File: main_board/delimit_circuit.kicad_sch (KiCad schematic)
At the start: 18 parts, among them J1 Conn_02x24_Counter_Clockwise, J2 Conn_02x24_Counter_Clockwise, J5 Screw_Terminal_01x02, J6 Screw_Terminal_01x02, J7 Screw_Terminal_01x02, J8 Screw_Terminal_01x02, U1 LTV-817, U2 LTV-817, U3 LTV-817, U4 LTV-817

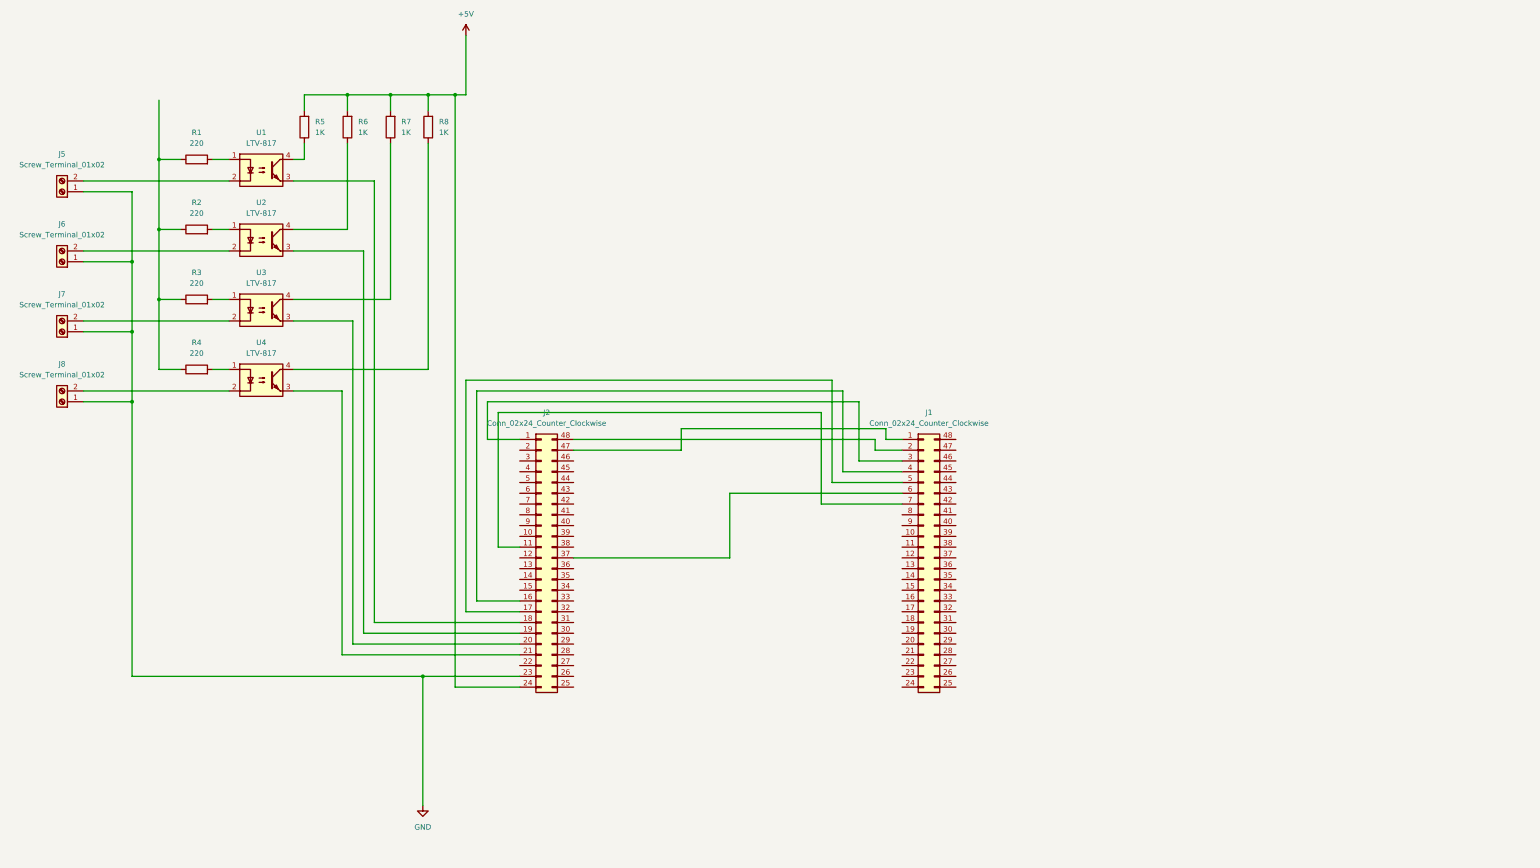
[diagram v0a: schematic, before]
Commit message: made teensy symbol
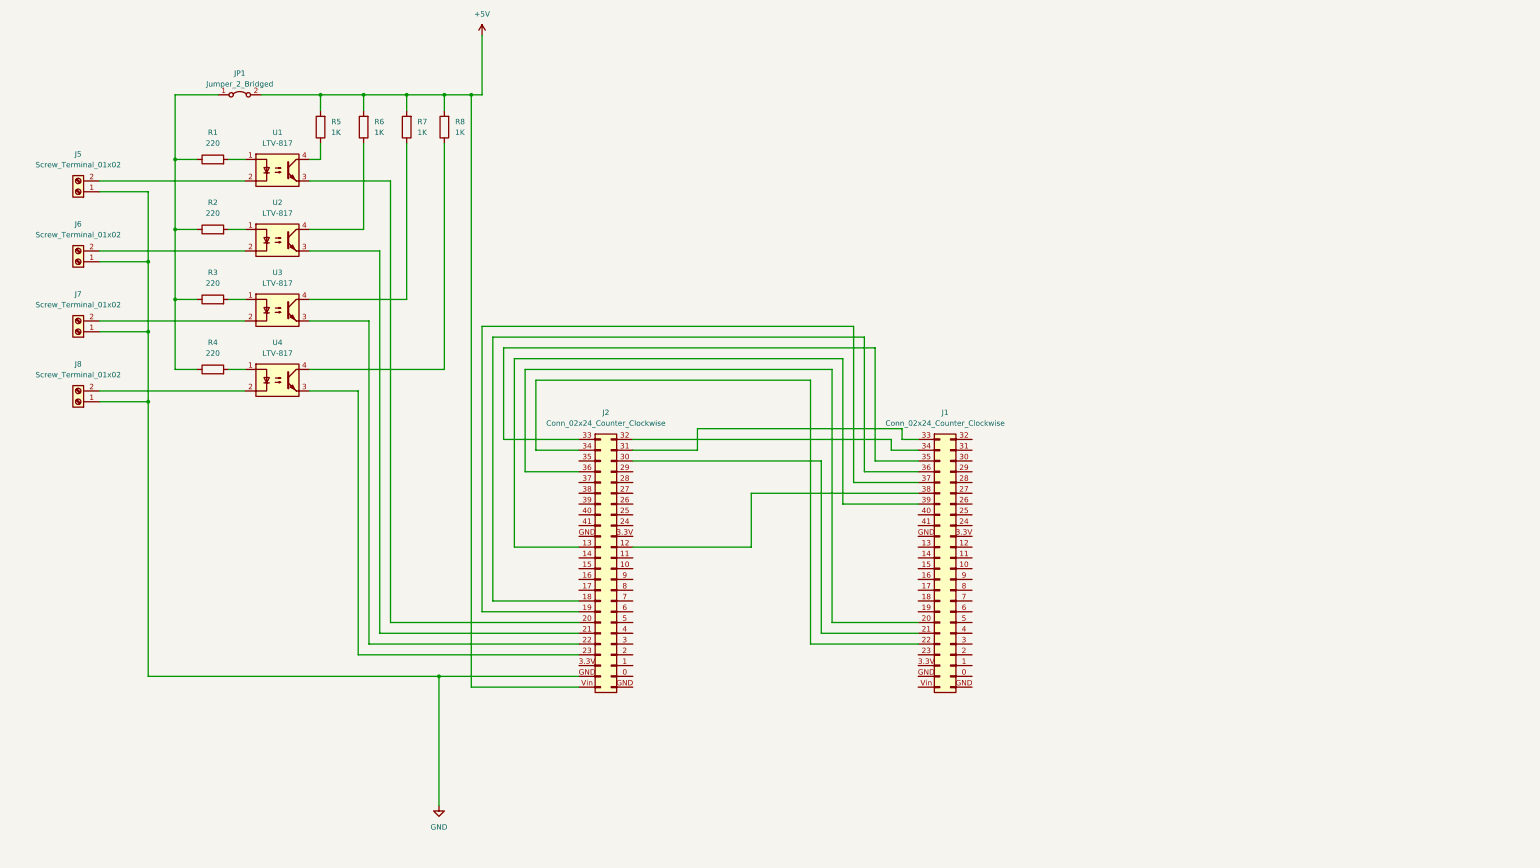
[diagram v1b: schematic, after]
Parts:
- added JP1: Jumper_2_Bridged, Jumper:SolderJumper-2_P1.3mm_Bridged2Bar_Pad1.0x1.5mm, symbol Jumper:Jumper_2_Bridged
- J1, J2: symbol Connector_Generic:Conn_02x24_Counter_Clockwise -> delimit:teensy_4_1_conn_02x24
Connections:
- net +5V: now also J2.Vin (Pin_Vin), JP1.2 (B); no longer J2.24 (Pin_24)
- net GND: now also J2.GND (Pin_GND); no longer J2.23 (Pin_23)
- net at R1.1, R2.1, R3.1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: now also JP1.1 (A)
- net at J2.1 (Pin_1): no longer J1.3 (Pin_3)
- net at J2.11 (Pin_11): no longer J1.7 (Pin_7)
- net at J2.12 (Pin_12): now also J1.38 (Pin_38)
- net at J2.13 (Pin_13): now also J1.39 (Pin_39)
- net at J2.16 (Pin_16): no longer J1.4 (Pin_4)
- net at J2.17 (Pin_17): no longer J1.5 (Pin_5)
- net at J2.18 (Pin_18): now also J1.36 (Pin_36); no longer U1.3
- net at J2.19 (Pin_19): now also J1.37 (Pin_37); no longer U2.3
- net at J2.20 (Pin_20): now also U1.3; no longer U3.3
- net at J2.21 (Pin_21): now also U2.3; no longer U4.3
- net at J2.22 (Pin_22): now also U3.3
- net at J2.30 (Pin_30): now also J1.21 (Pin_21)
- net at J2.31 (Pin_31): now also J1.33 (Pin_33)
- net at J2.32 (Pin_32): now also J1.34 (Pin_34)
- net at J2.33 (Pin_33): now also J1.35 (Pin_35)
- net at J2.34 (Pin_34): now also J1.22 (Pin_22)
- net at J2.36 (Pin_36): now also J1.20 (Pin_20)
- net at J2.37 (Pin_37): no longer J1.6 (Pin_6)
- net at J1.1 (Pin_1): no longer J2.47 (Pin_47)
- net at J1.2 (Pin_2): no longer J2.48 (Pin_48)
- new net: J2.23 (Pin_23), U4.3
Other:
- moved on the sheet: J1, J2, J5, J6, J7, J8, R1, R2, R3, R4, R5, R6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

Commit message: save
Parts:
- removed JP1: Jumper_2_Bridged, Jumper:SolderJumper-2_P1.3mm_Bridged2Bar_Pad1.0x1.5mm, symbol Jumper:Jumper_2_Bridged
- added C1, C2: C_Polarized, Capacitor_THT:CP_Radial_D4.0mm_P2.00mm, symbol Device:C_Polarized
- added J10: step_t3, symbol delimit:stepper_driver_conn_02x08
- added J11: step_t2, symbol delimit:stepper_driver_conn_02x08
- added J12, J13, J14, J15: step_t3, TerminalBlock_Phoenix:TerminalBlock_Phoenix_MKDS-1,5-2_1x02_P5.00mm_Horizontal, symbol Connector:Screw_Terminal_01x02
- added J3: e_stop, TerminalBlock_Phoenix:TerminalBlock_Phoenix_MKDS-1,5-2_1x02_P5.00mm_Horizontal, symbol Connector:Screw_Terminal_01x02
- added J4: therm_t3, TerminalBlock_Phoenix:TerminalBlock_Phoenix_MKDS-1,5-2_1x02_P5.00mm_Horizontal, symbol Connector:Screw_Terminal_01x02
- added J9: therm_t2, TerminalBlock_Phoenix:TerminalBlock_Phoenix_MKDS-1,5-2_1x02_P5.00mm_Horizontal, symbol Connector:Screw_Terminal_01x02
- added R10: 220, Resistor_THT:R_Axial_DIN0204_L3.6mm_D1.6mm_P5.08mm_Horizontal, symbol Device:R
- added R11, R12, R13, R14, R15, R16, R9: 4.7K, Resistor_THT:R_Axial_DIN0204_L3.6mm_D1.6mm_P5.08mm_Horizontal, symbol Device:R
- added U5: LTV-817, Package_DIP:DIP-4_W7.62mm, symbol Isolator:LTV-817
- J1: value Conn_02x24_Counter_Clockwise -> aux_control
- J2: value Conn_02x24_Counter_Clockwise -> grbl
- J5: value Screw_Terminal_01x02 -> switch_a
- J6: value Screw_Terminal_01x02 -> switch_z
- J7: value Screw_Terminal_01x02 -> switch_y
- J8: value Screw_Terminal_01x02 -> switch_x
- R5, R6, R7, R8: value 1K -> 4.7K
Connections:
- net +5V: now also R1.1, R2.1, R3.1, R4.1, J10.GND (Pin_GND), J10.MS1 (Pin_MS1), J10.VIO (Pin_VIO), J11.GND (Pin_GND), J11.MS1 (Pin_MS1), J11.VIO (Pin_VIO), R10.1, R9.2
- net GND: now also U1.3, U2.3, U3.3, U4.3, C1.2, C2.2, J10.GND (Pin_GND), J10.MS2 (Pin_MS2), J11.GND (Pin_GND), J11.MS2 (Pin_MS2), J3.1 (Pin_1), J4.1 (Pin_1), J9.1 (Pin_1), R11.2, R12.2, R13.2, R14.1, U5.3
- net at J2.14 (Pin_14): now also R9.1, U5.4
- net at J2.15 (Pin_15): now also R11.1
- net at J2.16 (Pin_16): now also R12.1
- net at J2.17 (Pin_17): now also R13.1
- net at J2.20 (Pin_20): now also R8.1, U4.4; no longer U1.3
- net at J2.21 (Pin_21): now also R7.1, U3.4; no longer U2.3
- net at J2.22 (Pin_22): now also R6.1, U2.4; no longer U3.3
- net at J2.23 (Pin_23): now also R5.1, U1.4; no longer U4.3
- net at J2.28 (Pin_28): now also R14.2
- net at J1.14 (Pin_14): now also C2.1, J9.2 (Pin_2), R16.2
- net at J1.15 (Pin_15): now also C1.1, J4.2 (Pin_2), R15.2
- net at J1.24 (Pin_24): now also J11.DIR (Pin_DIR)
- net at J1.25 (Pin_25): now also J11.STEP (Pin_STEP)
- net at J1.26 (Pin_26): now also J11.EN (Pin_EN)
- net at J1.27 (Pin_27): now also J10.DIR (Pin_DIR)
- net at J1.28 (Pin_28): now also J10.STEP (Pin_STEP)
- net at J1.29 (Pin_29): now also J10.EN (Pin_EN)
- new net: J10.M2A (Pin_M2A), J12.1 (Pin_1)
- new net: J10.M2B (Pin_M2B), J12.2 (Pin_2)
- new net: R10.2, U5.1
- new net: J3.2 (Pin_2), U5.2
- new net: J11.M1B (Pin_M1B), J14.1 (Pin_1)
- new net: J11.M1A (Pin_M1A), J14.2 (Pin_2)
- new net: J10.M1B (Pin_M1B), J13.1 (Pin_1)
- new net: J10.M1A (Pin_M1A), J13.2 (Pin_2)
- new net: J1.3.3V (Pin_3.3V), R15.1, R16.1
- new net: J11.M2A (Pin_M2A), J15.1 (Pin_1)
- new net: J11.M2B (Pin_M2B), J15.2 (Pin_2)
- new net +24V: J10.Vmot (Pin_Vmot), J11.Vmot (Pin_Vmot)
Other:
- moved on the sheet: J1, J2, J5, J6, J7, J8, R1, R2, R3, R4, R5, R6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
